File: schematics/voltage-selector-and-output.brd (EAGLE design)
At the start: 40.3 x 24.1 mm, 25 parts, among them IC2 Tiny85-20-SMT, IC3 MCP41010P, IC4 5V, IC5 MIC2941, X1 USB-A-H

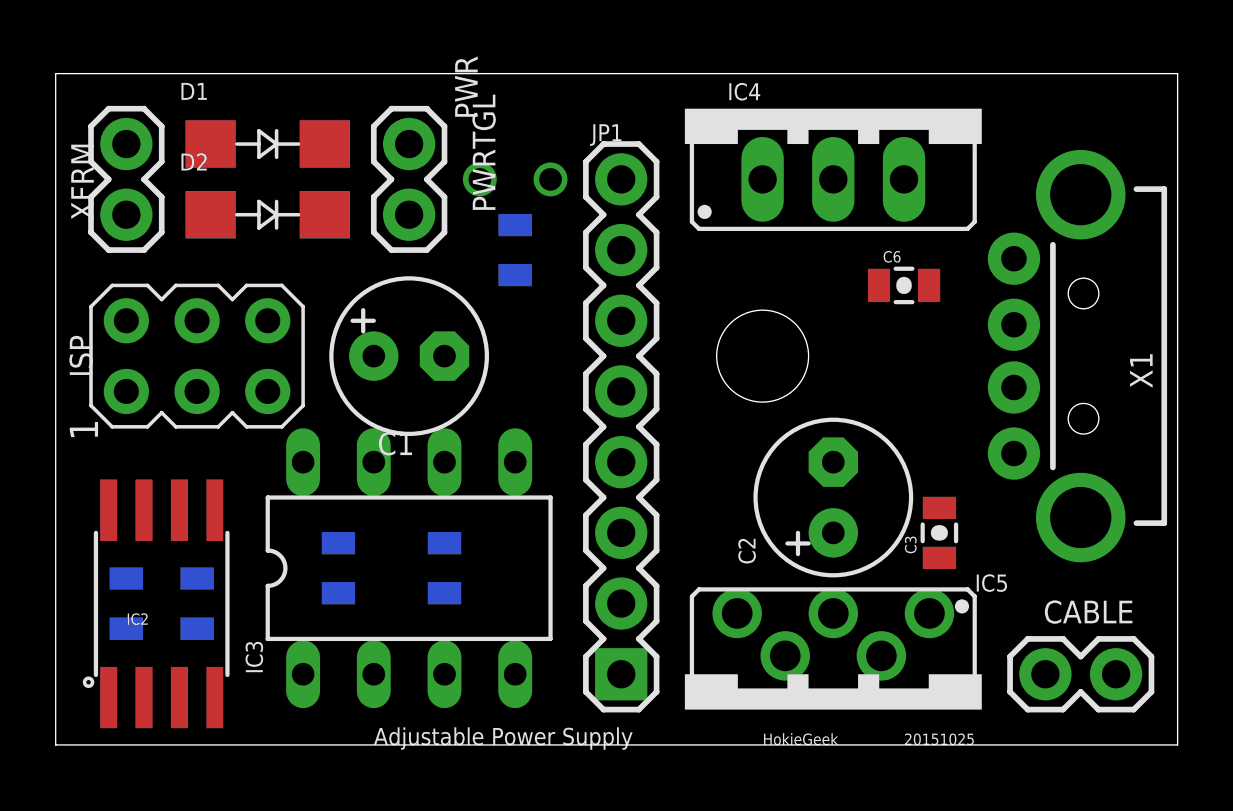
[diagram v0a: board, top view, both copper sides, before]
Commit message: This version's autorouter is way better than the older
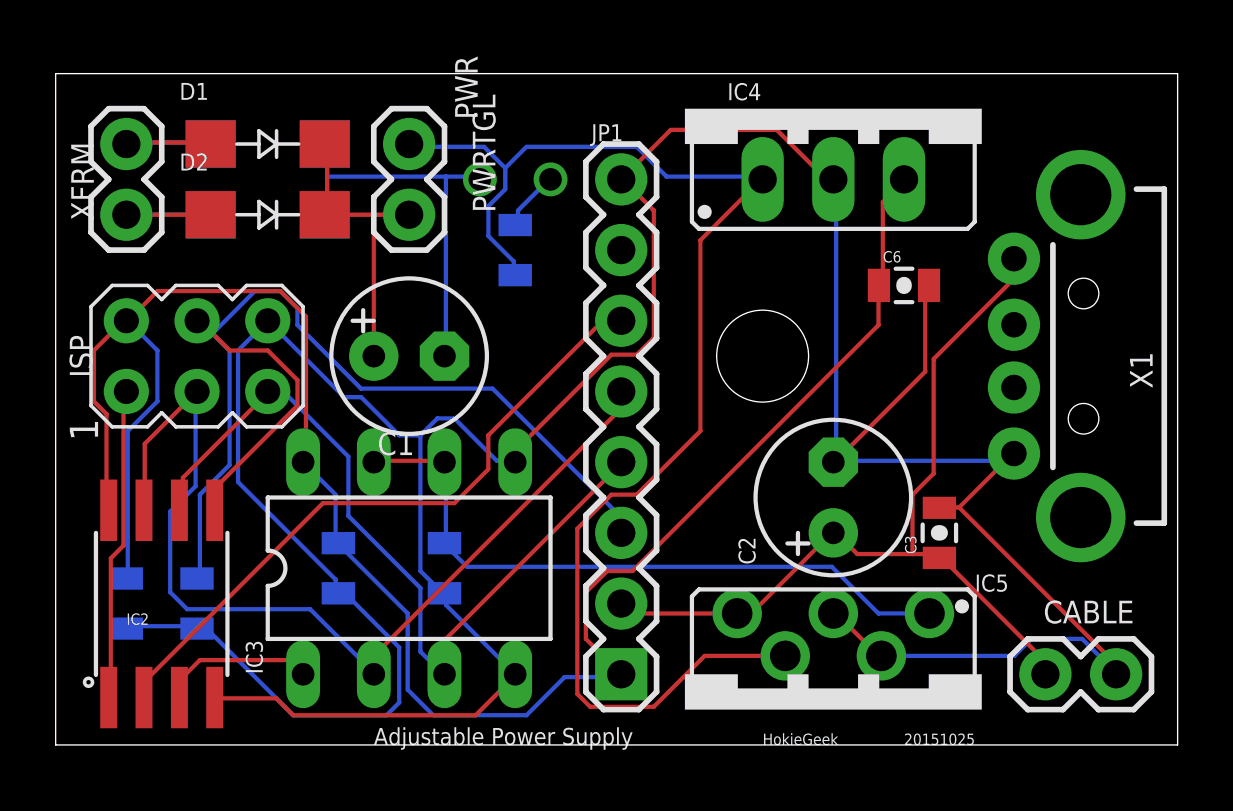
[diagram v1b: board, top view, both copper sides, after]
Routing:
- net AGND: track 0.00 -> 131.7 mm
- net VIC: track 0.00 -> 72.3 mm
- net VCC: track 0.00 -> 48.6 mm
- net PB0: track 0.00 -> 41.0 mm
- net PB2: track 0.00 -> 35.1 mm
- net VADJ: track 0.00 -> 31.1 mm
- net PB1: track 0.00 -> 29.0 mm
- net N$1: track 0.00 -> 24.0 mm
- net PB3: track 0.00 -> 23.8 mm
- net N$5: track 0.00 -> 14.7 mm
- net PB5: track 0.00 -> 11.3 mm
- net N$9: track 0.00 -> 10.7 mm
- net N$2: track 0.00 -> 6.13 mm
- net GND: track 0.00 -> 6.06 mm
- net PB4: track 0.00 -> 5.57 mm
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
